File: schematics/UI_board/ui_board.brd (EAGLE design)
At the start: 100 x 80 mm, 52 parts, among them IC1 74HCT00N, IC10 74HCT32N, IC11 74HCT14N, IC12 74HCT14N, IC2 74HCT151N, IC3 74HCT174N, IC4 74HCT74N, IC5 74HCT04N, IC6 74HCT08N, IC7 74HC148N, IC8 74HCT373N, IC9 74HCT32N

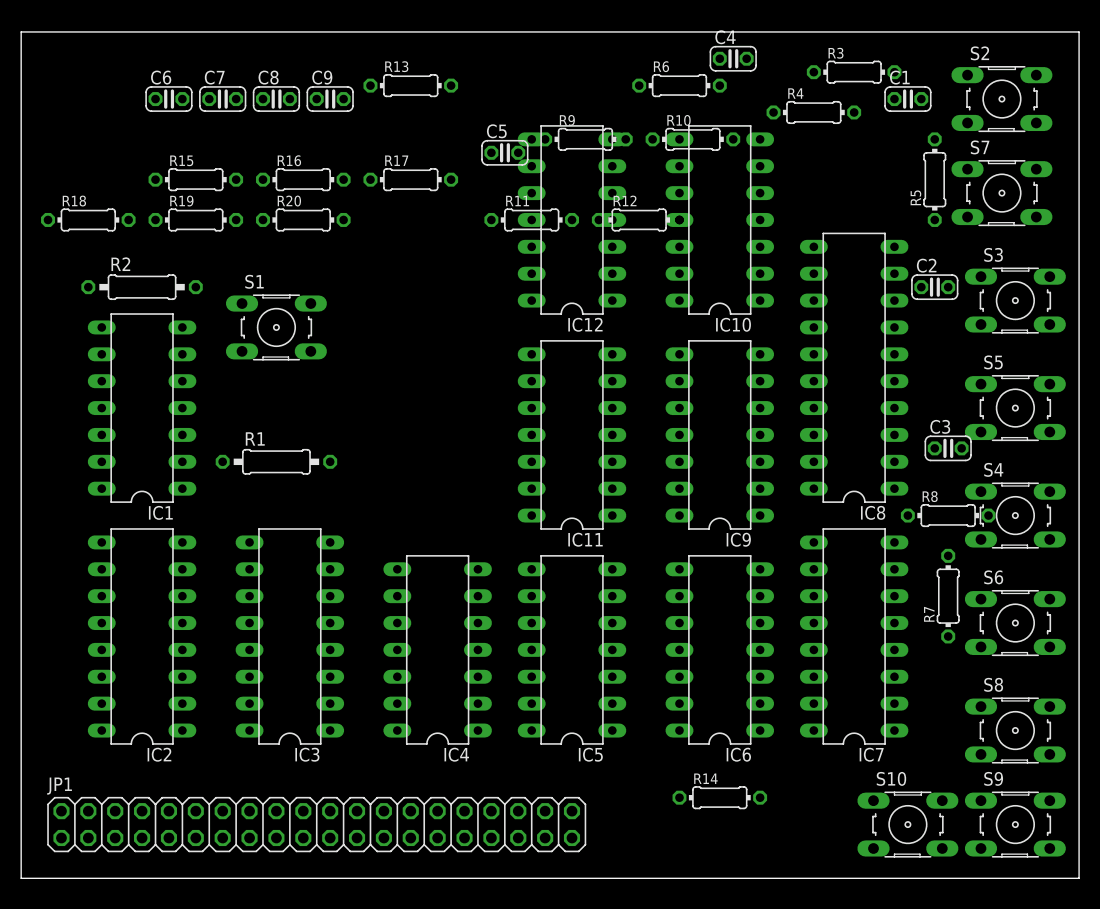
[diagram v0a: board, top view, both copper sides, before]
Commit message: changed register chips to 74xx374
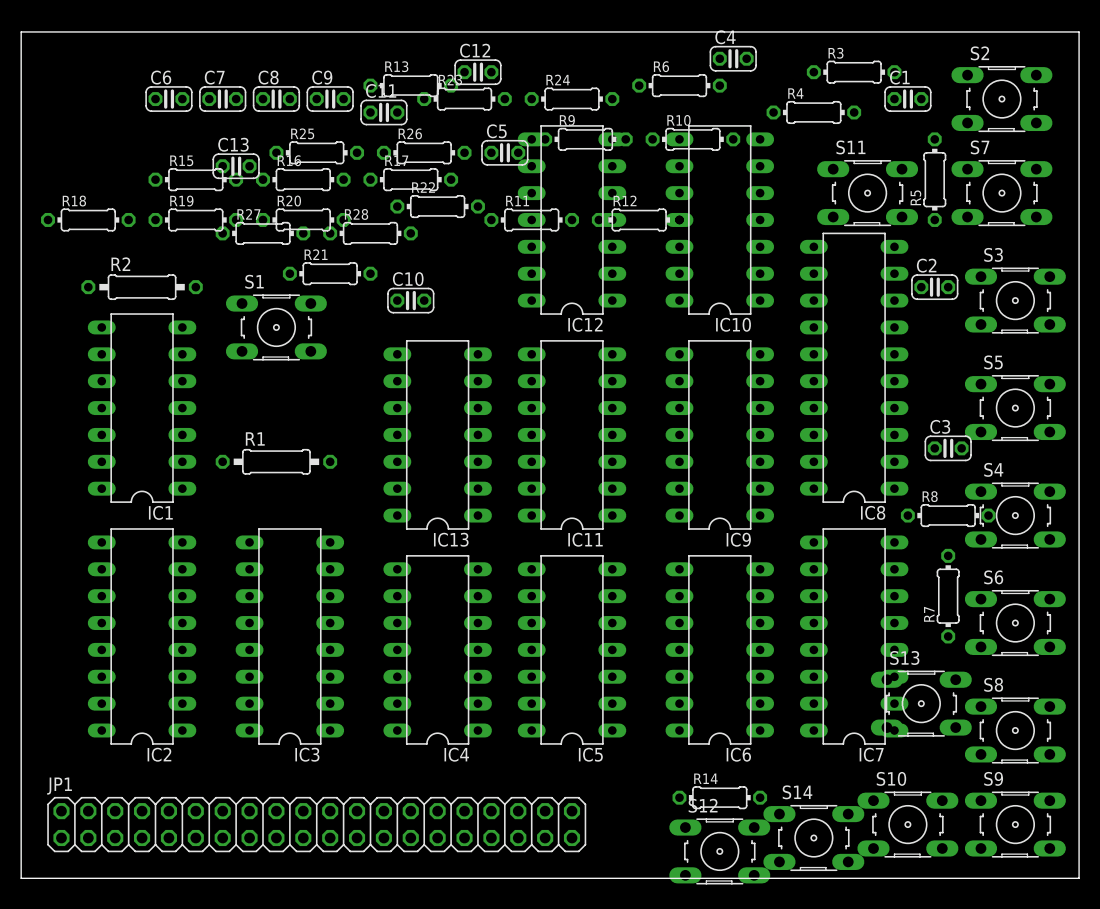
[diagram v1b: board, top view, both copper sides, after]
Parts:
- added C10, C11, C12, C13: 1µF, rcl:C025-024X044
- added IC13: 74HCT14N, 74xx-eu:DIL14
- added R21, R23, R25, R27: 10k, rcl:0204/7
- added R22, R24, R26, R28: 22k, rcl:0204/7
- added S11, S12, S13, S14: (no value), switch-omron:B3F-10XX
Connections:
- removed net N$17: IC7.5
- new net CHANGE_CLOCK_SELECT10: IC12.4, IC5.9
- new net CHANGE_CLOCK_SELECT11: IC13.8, IC5.11
- new net CHANGE_CLOCK_SELECT4: IC12.8, IC5.3
- new net CHANGE_CLOCK_SELECT9: IC12.2, IC5.5
- new net N$48: R23.1, R24.1, S12.1, S12.2
- new net N$50: R21.1, R22.1, S11.1, S11.2
- new net N$51: C10.1, IC12.9, R22.2
- new net N$52: C11.1, IC12.1, R24.2
- new net N$53: R25.1, R26.1, S13.1, S13.2
- new net N$54: C12.1, IC12.3, R26.2
- new net N$55: R27.1, R28.1, S14.1, S14.2
- new net N$56: C13.1, IC13.9, R28.2
- net !CLR_CARRY_BIT: now also IC5.8
- net !REGISTER_RESET: now also IC5.4
- net !RING_CNTR_RESET: now also IC5.6
- net !SET_CARRY_BIT: now also IC5.10
- net GND: now also C10.2, C11.2, C12.2, C13.2, IC13.7, IC7.5, S11.3, S11.4, S12.3, S12.4, S13.3, S13.4, S14.3, S14.4
- net VCC: now also IC13.14, R21.2, R23.2, R25.2, R27.2

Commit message: start ui board layout
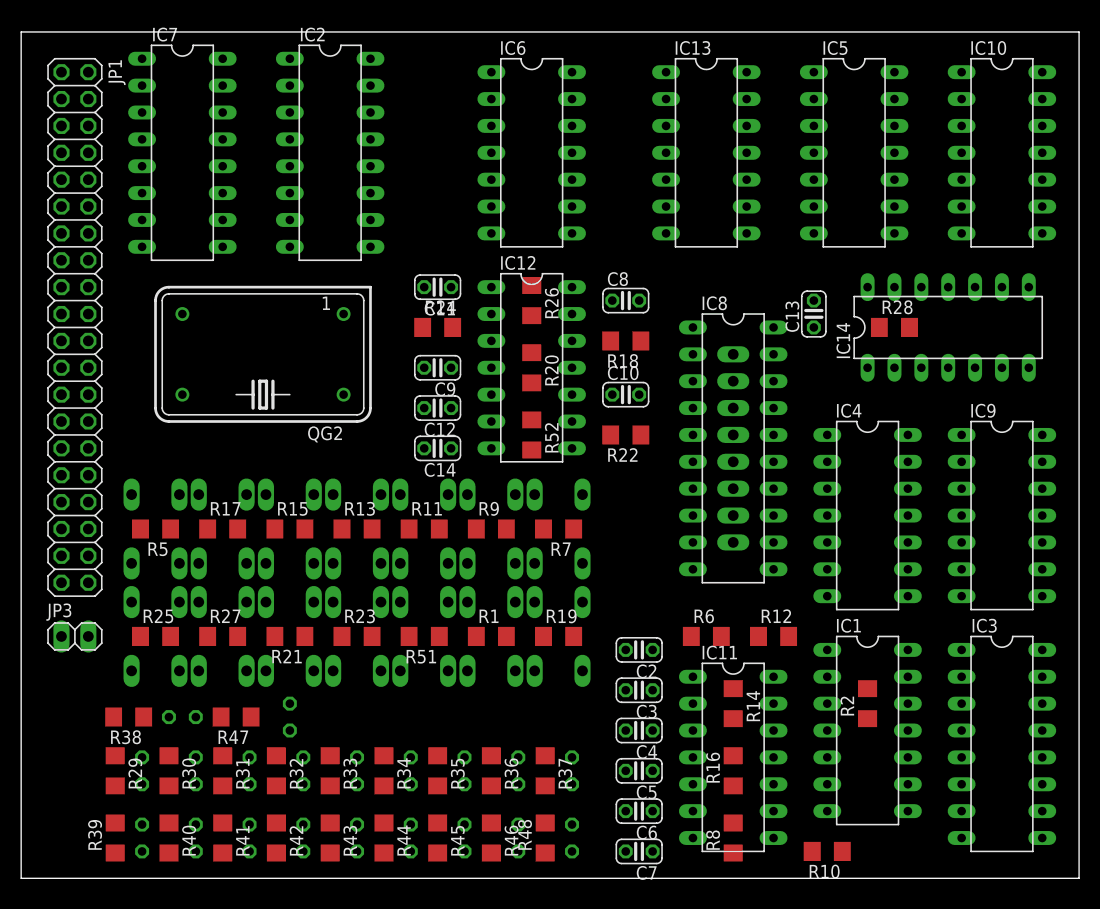
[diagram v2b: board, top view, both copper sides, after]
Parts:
- removed C1: 1µF, rcl:C025-024X044
- removed R3: 10k, rcl:0204/7
- removed R4: 22k, rcl:0204/7
- removed S2: (no value), switch-omron:B3F-10XX
- added C14: 1µF, rcl:C025-024X044
- added IC14: 74HCT14N, 74xx-eu:DIL14
- added JP2: (no value), pinhead:1X08
- added JP3: (no value), pinhead:1X02
- added LED1, LED10, LED11, LED12, LED13, LED14, LED15, LED16, LED17, LED18, LED19, LED2, LED20, LED3, LED4, LED5, LED6, LED7, LED8, LED9: (no value), led:LED3MM
- added QG2: (no value), crystal:DIL14S
- added R29, R30, R31, R32, R33, R34, R35, R36, R37, R38, R39, R40, R41, R42, R43, R44, R45, R46, R47, R48, R52: 22k, rcl:R1206
- added R51: 10k, rcl:R1206
- added S16: (no value), switch-omron:B3F-10XX
- IC13: value 74HCT14N -> 74HCT393N
- R1, R2: device rcl:0207/10 -> rcl:R1206
- R10, R11, R12, R13, R14, R15, R16, R17, R18, R19, R20, R21, R22, R23, R24, R25, R26, R27, R28, R5, R6, R7, R8, R9: device rcl:0204/7 -> rcl:R1206
- moved S3 84.1 mm to (12.7, 33.0), flipped to the bottom, turned to 90 degrees
- moved C7 81.3 mm to (58.4, 2.54), turned to 180 degrees
- moved R5 80.7 mm to (12.7, 33.0), turned to 180 degrees
- moved C6 80.7 mm to (58.4, 6.35), turned to 180 degrees
- moved S9 80.0 mm to (19.1, 33.0), flipped to the bottom, turned to 90 degrees
- moved R2 79.1 mm to (80.0, 16.5), turned to 90 degrees
- moved IC7 78.2 mm to (15.2, 68.6), turned to 270 degrees
- moved IC1 75.0 mm to (80.0, 14.0), turned to 270 degrees
- moved S13 72.7 mm to (12.7, 22.9), flipped to the bottom, turned to 90 degrees
- moved S8 71.2 mm to (25.4, 33.0), flipped to the bottom, turned to 270 degrees
- moved R16 69.1 mm to (67.3, 10.2), turned to 90 degrees
- moved S11 68.8 mm to (25.4, 22.9), flipped to the bottom, turned to 90 degrees
- moved S7 68.7 mm to (31.8, 33.0), flipped to the bottom, turned to 90 degrees
- moved R10 68.5 mm to (76.2, 2.54), turned to 180 degrees
- moved IC3 68.1 mm to (92.7, 12.7), turned to 270 degrees
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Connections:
- removed net 100KHZ: IC2.2
- removed net 10HZ: IC2.3
- removed net 12MHZ: IC2.12
- removed net N$32: IC8.11, IC9.3
- removed net N$33: R3.1, R4.1, S2.1, S2.2
- removed net N$34: C1.1, IC12.5, R4.2
- new net 31.25KHZ: IC13.8, IC2.3
- new net 500KHZ: IC13.13, IC13.6, IC2.2
- new net N$17: LED20.K, R38.1
- new net N$57: LED10.K, R39.2
- new net N$58: LED12.K, R40.2
- new net N$59: LED13.K, R41.2
- new net N$60: LED2.K, R29.2
- new net N$61: LED1.K, R30.2
- new net N$62: LED3.K, R31.2
- new net N$63: LED4.K, R32.2
- new net N$64: LED5.K, R33.2
- new net N$65: LED6.K, R34.2
- new net N$66: LED7.K, R35.2
- new net N$67: LED8.K, R36.2
- new net N$68: LED9.K, R37.2
- new net N$69: LED14.K, R42.2
- new net N$70: LED15.K, R43.2
- new net N$71: LED16.K, R44.2
- new net N$72: LED17.K, R45.2
- new net N$73: LED18.K, R46.2
- new net N$74: LED19.K, R47.1
- new net N$75: LED11.K, R48.1
- new net N$79: R51.1, R52.1, S16.1, S16.2
- new net N$80: C14.1, IC12.5, R52.2
- net !RESET_CLOCK_SELECT: now also IC12.6
- net 1MHZ: now also IC13.5
- net 2MHZ: now also IC13.4
- net 4MHZ: now also IC13.3
- net 8MHZ: now also IC13.1, QG2.8
- net ALU_CARRY_BIT: now also LED11.A
- net CHANGE_CLOCK_SELECT: now also IC8.11, IC9.3; no longer IC12.6
- net CHANGE_CLOCK_SELECT11: now also IC14.10; no longer IC13.8
- net CYCL_1: now also LED2.A
- net CYCL_2: now also LED1.A
- net CYCL_3: now also LED3.A
- net CYCL_4: now also LED4.A
- net CYCL_5: now also LED5.A
- net CYCL_6: now also LED6.A
- net CYCL_7: now also LED7.A
- net CYCL_8: now also LED8.A
- net CYCL_9: now also LED9.A
- net GND: now also C14.2, IC13.12, IC13.2, IC14.7, IC2.12, JP3.1, QG2.7, R29.1, R30.1, R31.1, R32.1, R33.1, R34.1, R35.1, R36.1, R37.1, R38.2, R39.1, R40.1, R41.1, R42.1, R43.1, R44.1, R45.1, R46.1, R47.2, R48.2, S16.3, S16.4; no longer C1.2, S2.3, S2.4
- net N$18: now also JP2.1
- net N$19: now also JP2.2
- net N$20: now also JP2.3
- net N$21: now also JP2.4
- net N$22: now also JP2.5
- net N$23: now also JP2.6
- net N$24: now also JP2.7
- net N$25: now also JP2.8
- net N$56: now also IC14.11; no longer IC13.9
- net REG0_OUT_0: now also LED10.A
- net REG0_OUT_1: now also LED12.A
- net REG0_OUT_2: now also LED13.A
- net REG0_OUT_3: now also LED14.A
- net REG0_OUT_4: now also LED15.A
- net REG0_OUT_5: now also LED16.A
- net REG0_OUT_6: now also LED17.A
- net REG0_OUT_7: now also LED18.A
- net REG0_ZERO: now also LED20.A
- net SP_DATA_OVER/UNDERFLOW: now also LED19.A
- net VCC: now also IC14.14, QG2.14, R51.2; no longer R3.2

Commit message: fix. gonna try to reduce cycles to 8 per instruction now
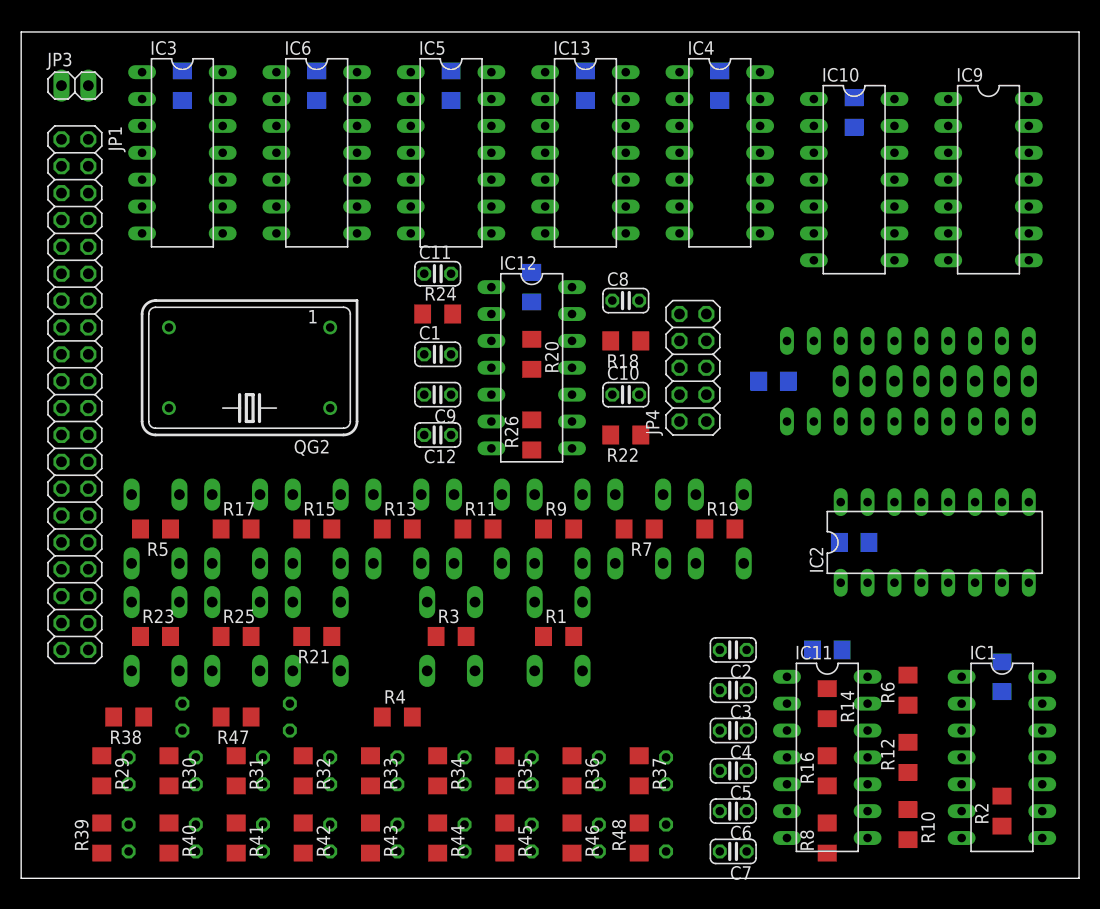
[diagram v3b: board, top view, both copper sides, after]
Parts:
- removed IC14: 74HCT14N, 74xx-eu:DIL14
- removed IC7: 74HC148N, 74xx-eu:DIL16
- removed R27, R51: 10k, rcl:R1206
- removed R28, R52: 22k, rcl:R1206
- removed S14, S16: (no value), switch-omron:B3F-10XX
- added C1: 1µF, rcl:C025-024X044
- added C15, C16, C17, C18, C19, C20, C21, C22, C23: (no value), rcl:C1206
- added JP4: (no value), pinhead:2X05
- added R3: 10k, rcl:R1206
- added R4: 22k, rcl:R1206
- added S2: (no value), switch-omron:B3F-10XX
- C13, C14: value 1µF -> (none); device rcl:C025-024X044 -> rcl:C1206
- IC3: value 74HCT174N -> 74HCT32N; device 74xx-eu:DIL16 -> 74xx-eu:DIL14
- IC6: value 74HCT08N -> 74HCT32N
- moved IC3 95.5 mm to (15.2, 68.6)
- moved IC2 68.0 mm to (86.4, 31.8), turned to 0 degrees
- moved C13 63.5 mm to (15.2, 74.9), flipped to the bottom
- moved JP3 52.1 mm to (5.08, 74.9)
- moved IC5 38.1 mm to (40.6, 68.6)
- moved IC4 37.0 mm to (66.0, 68.6)
- moved C14 36.1 mm to (27.9, 74.9), flipped to the bottom, turned to 90 degrees
- moved IC9 31.8 mm to (91.4, 66.0)
- moved IC6 20.3 mm to (27.9, 68.6)
- moved JP2 20.1 mm to (86.4, 47.0), turned to 0 degrees
- moved R6 19.7 mm to (83.8, 17.8), turned to 90 degrees
- moved R23 19.1 mm to (12.7, 22.9)
- moved S12 19.1 mm to (12.7, 22.9)
- moved R19 18.3 mm to (66.0, 33.0)
- moved S10 18.3 mm to (66.0, 33.0)
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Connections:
- removed net !RESET_CLOCK_SELECT: IC12.6, IC3.1
- removed net CHANGE_CLOCK_SELECT10: IC12.4, IC5.9
- removed net CHANGE_CLOCK_SELECT11: IC14.10, IC5.11
- removed net CHANGE_CLOCK_SELECT4: IC12.8, IC5.3
- removed net CHANGE_CLOCK_SELECT9: IC12.2, IC5.5
- removed net N$54 (its old number): C12.1, IC12.3, R26.2
- removed net N$56: C13.1, IC14.11, R28.2
- removed net N$79: R51.1, R52.1, S16.1, S16.2
- removed net N$80: C14.1, IC12.5, R52.2
- new net N$32: IC3.8, IC6.10
- new net N$33: IC3.3, IC6.4
- new net N$34: IC6.3, IC6.5
- new net N$48: C1.1, IC12.3, R4.2
- new net N$76: IC3.4, IC8.6, JP2.3
- new net TIMER_CLOCK: JP1.3, JP4.10, JP4.2, JP4.4, JP4.6, JP4.8
- net !CLR_CARRY_BIT: now also IC12.2; no longer IC5.8
- net !REGISTER_RESET: now also IC12.6; no longer IC5.4
- net !RING_CNTR_RESET: now also IC12.4; no longer IC5.6
- net !SET_CARRY_BIT: now also IC12.8; no longer IC5.10
- net 1MHZ: now also JP4.5
- net 2MHZ: now also JP4.3
- net 31.25KHZ: now also JP4.9
- net 4MHZ: now also JP4.1
- net 500KHZ: now also JP4.7
- net ALU_CARRY_BIT: now also JP1.16; no longer JP1.7
- net CHANGE_CLOCK_SELECT: now also IC1.13; no longer IC3.9, IC6.2
- net GND: now also C15.2, C16.2, C17.2, C18.2, C19.2, C20.2, C21.2, C22.2, C23.2, IC3.7, IC8.1, JP1.11, JP1.13, JP1.7, JP1.9, R21.2, R23.2, R25.2, R3.2; no longer C10.2, C11.2, C12.2, IC14.7, IC3.8, IC7.5, IC7.8, JP1.16, JP1.18, JP1.20, JP1.3, S11.3, S11.4, S12.3, S12.4, S13.3, S13.4, S14.3, S14.4, S16.3, S16.4
- net N$1: now also IC1.4; no longer IC6.4
- net N$10: now also IC5.12; no longer IC6.3
- net N$11: now also IC2.11, IC6.8; no longer IC3.3, IC7.9
- net N$12: now also IC3.11, IC6.12, IC6.9; no longer IC3.4, IC7.7
- net N$13: now also IC2.9, IC6.6; no longer IC3.6, IC7.6
- net N$18: now also IC3.6, IC6.13; no longer IC7.10, IC8.2, JP2.1
- net N$19: now also IC3.10; no longer IC7.11
- net N$20: now also R3.1, R4.1, S2.1, S2.2; no longer IC7.12, IC8.6, JP2.3
- net N$21: now also IC3.13; no longer IC7.13
- net N$22: now also IC3.1; no longer IC7.1
- net N$23: now also IC3.2, IC3.9; no longer IC7.2
- net N$24: now also IC3.5, IC6.1; no longer IC7.3
- net N$25: now also IC3.12, IC6.2; no longer IC7.4
- net N$4: now also IC1.11, IC5.13; no longer IC2.11, IC3.2
- net N$51: now also IC12.5; no longer IC12.9
- net N$55: now also C12.1, IC12.9, R26.2; no longer R27.1, R28.1, S14.1, S14.2
- net N$6: now also IC6.11; no longer IC3.5
- net N$7: now also IC8.2, JP2.1; no longer IC2.9, IC3.7
- net N$8: now also IC1.12; no longer IC6.1
- net REG0_ZERO: now also JP1.20; no longer JP1.11
- net RING_CNTR_CLOCK: now also IC1.6; no longer IC6.6
- net SELECTED_CLOCK: now also IC1.5; no longer IC6.5
- net SP_DATA_OVER/UNDERFLOW: now also JP1.18; no longer JP1.9
- net VCC: now also C1.2, C10.2, C11.2, C12.2, C13.1, C14.1, C15.1, C16.1, C17.1, C18.1, C19.1, C20.1, C21.1, C22.1, C23.1, IC3.14, JP3.2, S11.3, S11.4, S12.3, S12.4, S13.3, S13.4, S2.3, S2.4; no longer IC14.14, IC3.16, IC7.16, R21.2, R23.2, R25.2, R27.2, R51.2

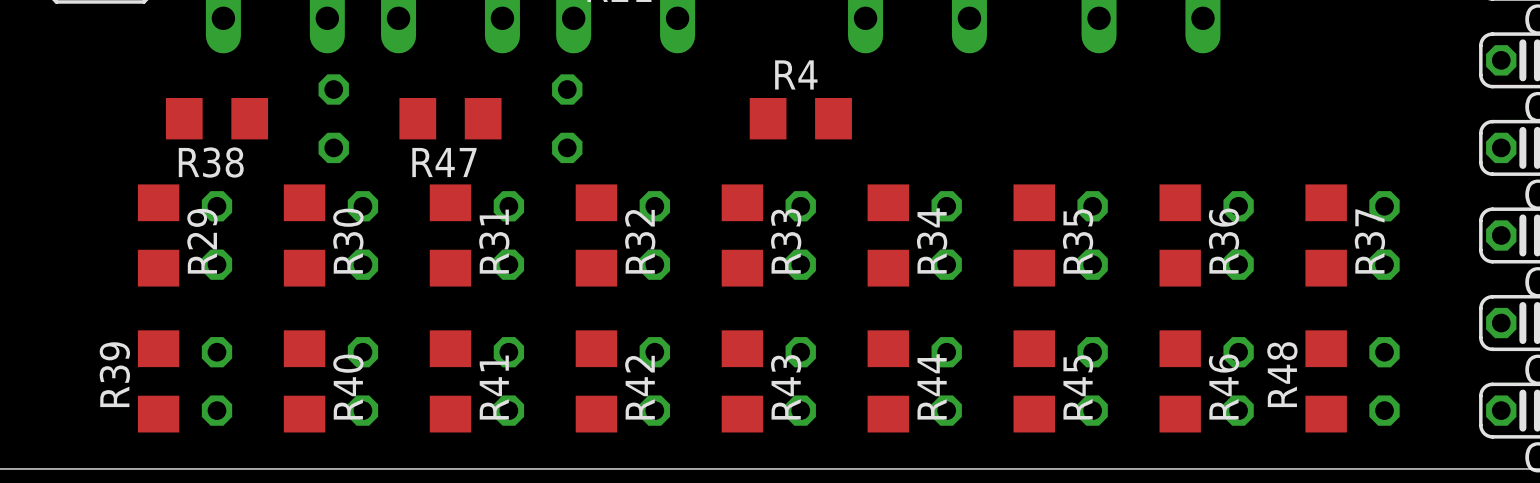
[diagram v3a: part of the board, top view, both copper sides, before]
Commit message: got rid of two cycles! finetuning next
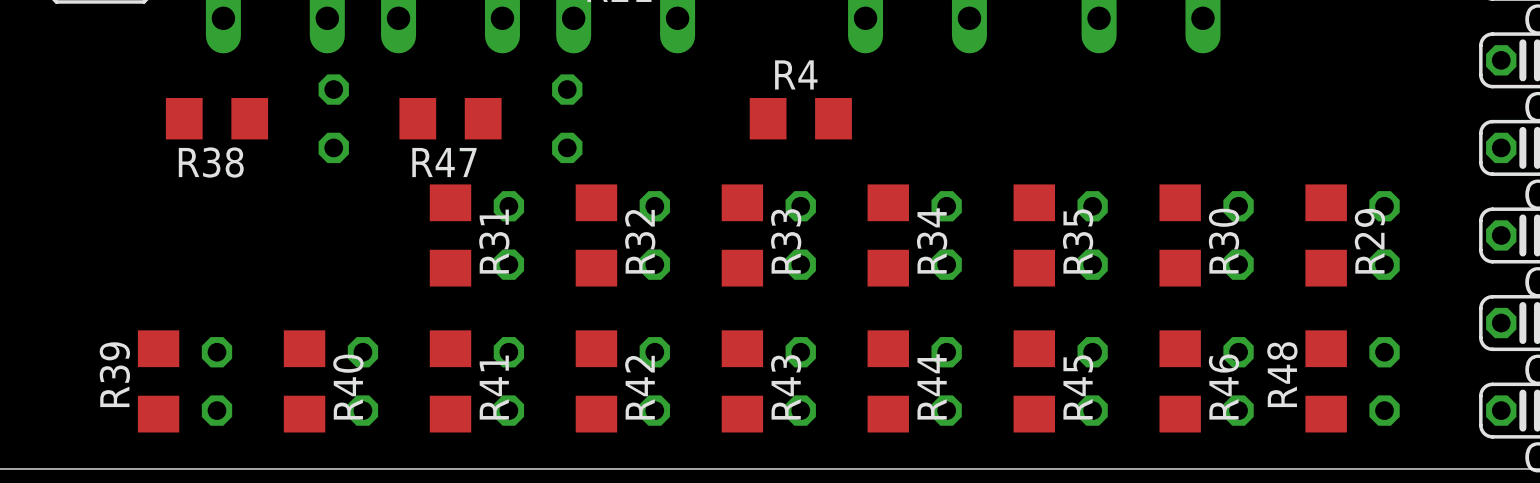
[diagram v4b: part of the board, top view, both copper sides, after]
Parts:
- removed LED8, LED9: (no value), led:LED3MM
- removed R36, R37: 22k, rcl:R1206
- moved R29 50.8 mm to (58.4, 10.2)
- moved R30 38.1 mm to (52.1, 10.2)
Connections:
- removed net CYCL_8: JP1.36, LED8.A
- removed net CYCL_9: JP1.38, LED9.A
- removed net N$67: LED8.K, R36.2
- removed net N$68: LED9.K, R37.2
- net GND: now also JP1.36, JP1.38; no longer R36.1, R37.1

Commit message: soldered ui bord
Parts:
- removed R2: (no value), rcl:R1206
- moved C14 26.2 mm to (17.8, 50.8), turned to 0 degrees
- moved IC5 24.3 mm to (24.1, 50.8), turned to 0 degrees
- moved C18 19.8 mm to (92.7, 45.7), turned to 270 degrees
- moved JP2 13.5 mm to (76.2, 38.1), turned to 270 degrees
- moved C20 12.0 mm to (77.5, 57.1), turned to 180 degrees
- moved QG2 11.5 mm to (22.9, 36.8)
- moved IC8 11.4 mm to (78.7, 36.8), flipped to the top, turned to 270 degrees
- moved IC9 10.8 mm to (83.8, 58.4), turned to 0 degrees
- moved C19 8.13 mm to (41.9, 50.8), turned to 0 degrees
- moved IC10 8.13 mm to (83.8, 72.4), turned to 0 degrees
- moved C15 7.62 mm to (33.0, 74.9)
- moved IC2 5.39 mm to (90.2, 35.6), turned to 270 degrees
- moved C16 5.08 mm to (48.3, 74.9)
- moved IC13 5.08 mm to (48.3, 68.6)
- moved IC6 5.08 mm to (33.0, 68.6)
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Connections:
- removed net N$3: IC1.10, R2.1, S1.2
- net GND: now also IC10.1, IC10.2, IC5.11, IC5.3, IC5.5, IC5.9
- net N$5: now also IC1.10, S1.2
- net VCC: no longer R2.2
